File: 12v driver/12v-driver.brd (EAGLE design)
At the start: 60.9 x 77.1 mm, 36 parts, among them IC1 74AC14N, IC2 74AC14N, Q1 2N3906, Q2 2N3906, Q3 IRFPC40, Q4 IRFPC40, T1 2N3904, T2 2N3904, T3 2N3904, T4 2N3904

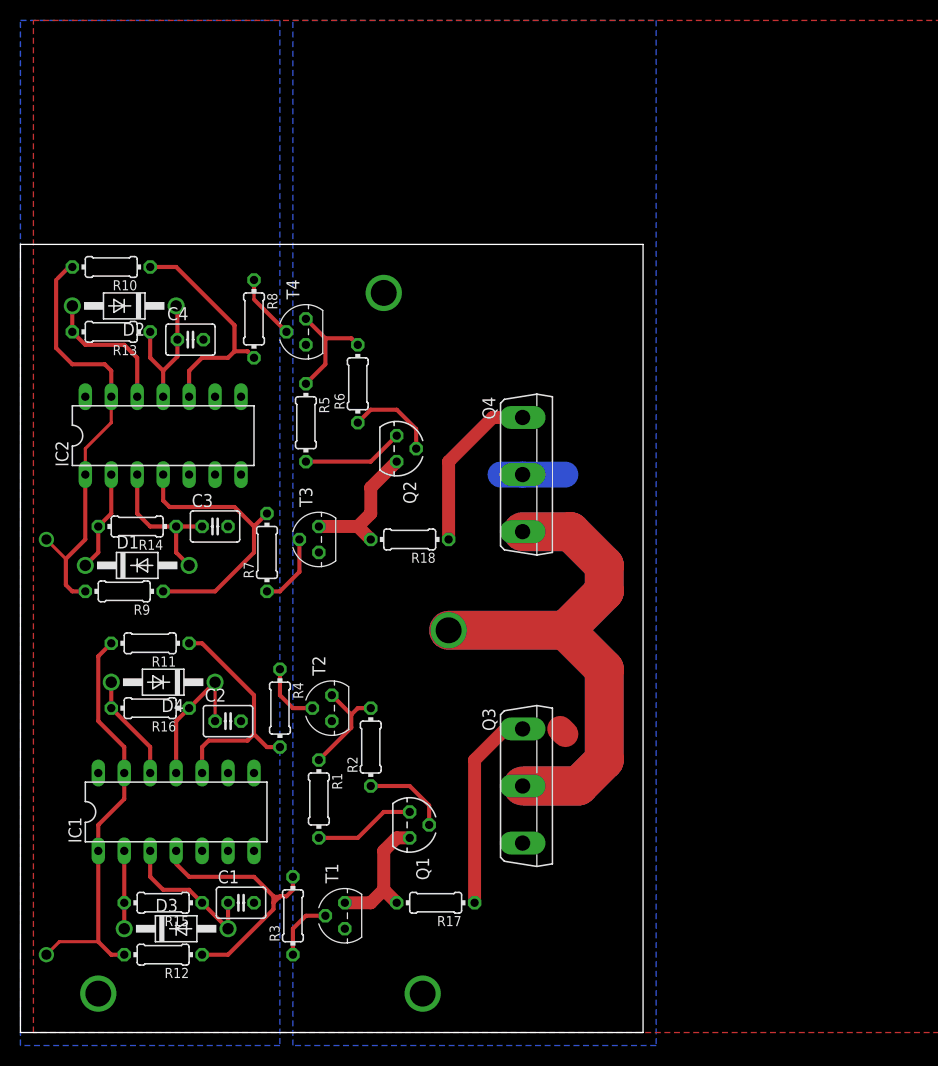
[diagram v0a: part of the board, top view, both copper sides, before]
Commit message: 12driver fix inversion and SMD
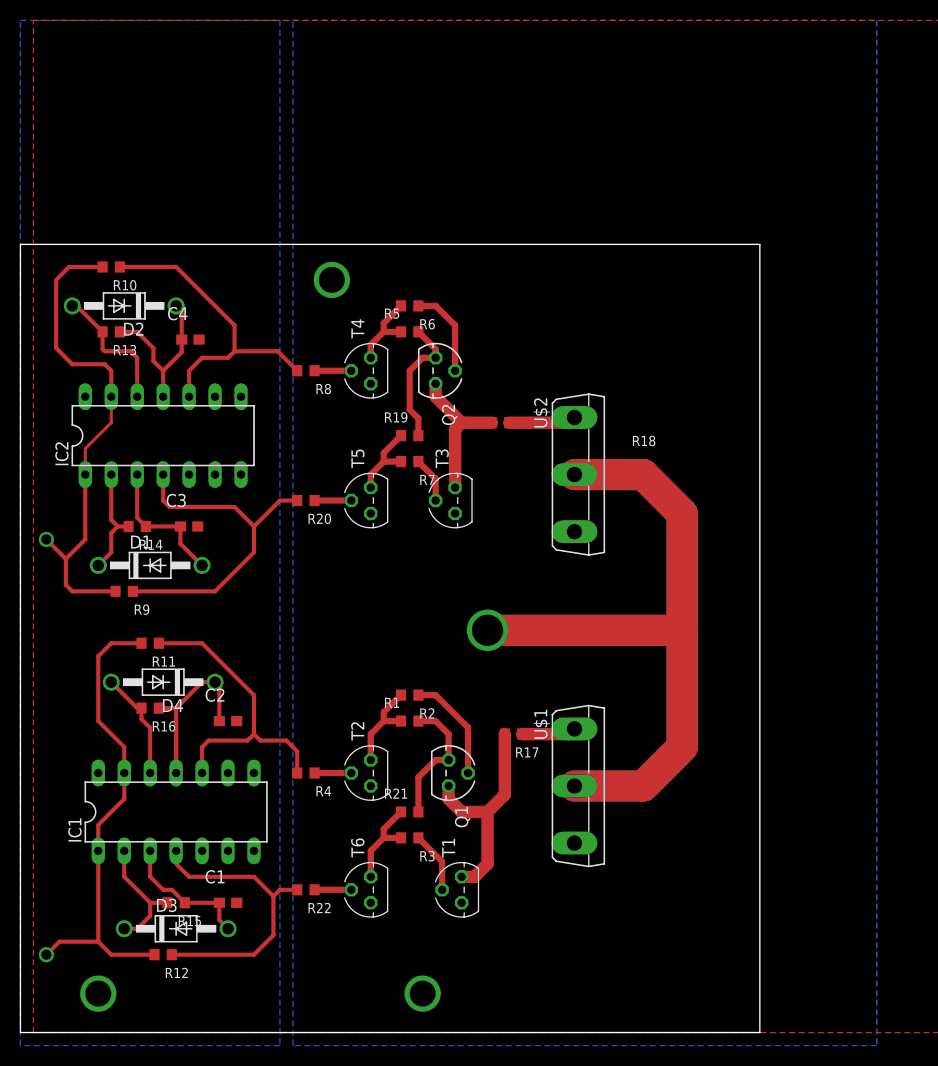
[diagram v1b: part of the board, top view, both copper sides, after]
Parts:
- removed Q3, Q4: IRFPC40, transistor-power:TO247BV
- added R19, R20, R21, R22: 1k, rcl:R0603
- added T5, T6: 2N3904, transistor:TO92
- added U$1: N-CHANNEL, transistors:TO247BV
- added U$2: P-CHANNEL, transistors:TO247BV
- C1, C2, C3, C4: device rcl:C025-030X050 -> rcl:C0603
- R1, R10, R11, R12, R13, R14, R15, R16, R17, R18, R2, R3, R4, R5, R6, R7, R8, R9: device rcl:0204/7 -> rcl:R0603
- moved R17 18.2 mm to (39.4, 29.2)
- moved R7 16.6 mm to (29.2, 55.9), turned to 180 degrees
- moved R18 14.5 mm to (38.1, 59.7)
- moved T3 13.9 mm to (33.7, 52.1)
- moved R3 13.7 mm to (29.2, 19.1), turned to 180 degrees
- moved R5 13.5 mm to (29.2, 68.6), turned to 0 degrees
- moved R1 11.7 mm to (29.2, 30.5), turned to 0 degrees
- moved T1 11.7 mm to (34.3, 14.0)
- moved R6 9.16 mm to (29.2, 71.1), turned to 180 degrees
- moved Q2 8.52 mm to (31.8, 64.8)
- moved T2 7.41 mm to (25.4, 25.4)
- moved T4 7.41 mm to (25.4, 64.8)
- moved R8 7.18 mm to (19.1, 64.8), turned to 180 degrees
- moved R4 6.84 mm to (19.1, 25.4), turned to 180 degrees
- moved R2 6.35 mm to (29.2, 33.0), turned to 180 degrees
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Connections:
- new net N$15: R20.1, T5.2
- new net N$24: R22.1, T6.2
- new net N$27: R19.1, R7.2, T5.1
- new net N$28: R21.1, R3.2, T6.1
- net GND: now also T5.3, T6.3, U$1.S; no longer Q3.S
- net N$14: now also R22.2; no longer R3.2
- net N$19: now also R20.2; no longer R7.2
- net N$2: now also U$1.G; no longer Q3.G
- net N$8: now also U$2.G; no longer Q4.G
- net OUTPUT: now also U$1.D, U$2.D; no longer Q3.D, Q4.S
- net V+: now also R19.2, R21.2, U$2.S; no longer Q4.D
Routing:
- net OUTPUT: track 104.1 -> 132.3 mm
- net N$2: track 19.9 -> 5.33 mm
- net N$8: track 16.6 -> 6.60 mm
- net N$28: track 0.00 -> 9.27 mm
- net N$1: track 13.0 -> 22.1 mm
- net N$27: track 0.00 -> 8.00 mm
- net N$21: track 23.1 -> 30.8 mm
- net N$16: track 14.3 -> 22.0 mm
- net N$17: track 23.5 -> 30.4 mm
- net N$19: track 27.3 -> 33.7 mm
- net IN2: track 42.8 -> 48.7 mm
- net IN1: track 40.5 -> 46.4 mm
- net N$25: track 7.62 -> 12.2 mm
- net N$24: track 0.00 -> 3.60 mm
- net N$15: track 0.00 -> 3.60 mm
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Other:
- board size 60.9 x 77.1 mm -> 72.4 x 77.1 mm

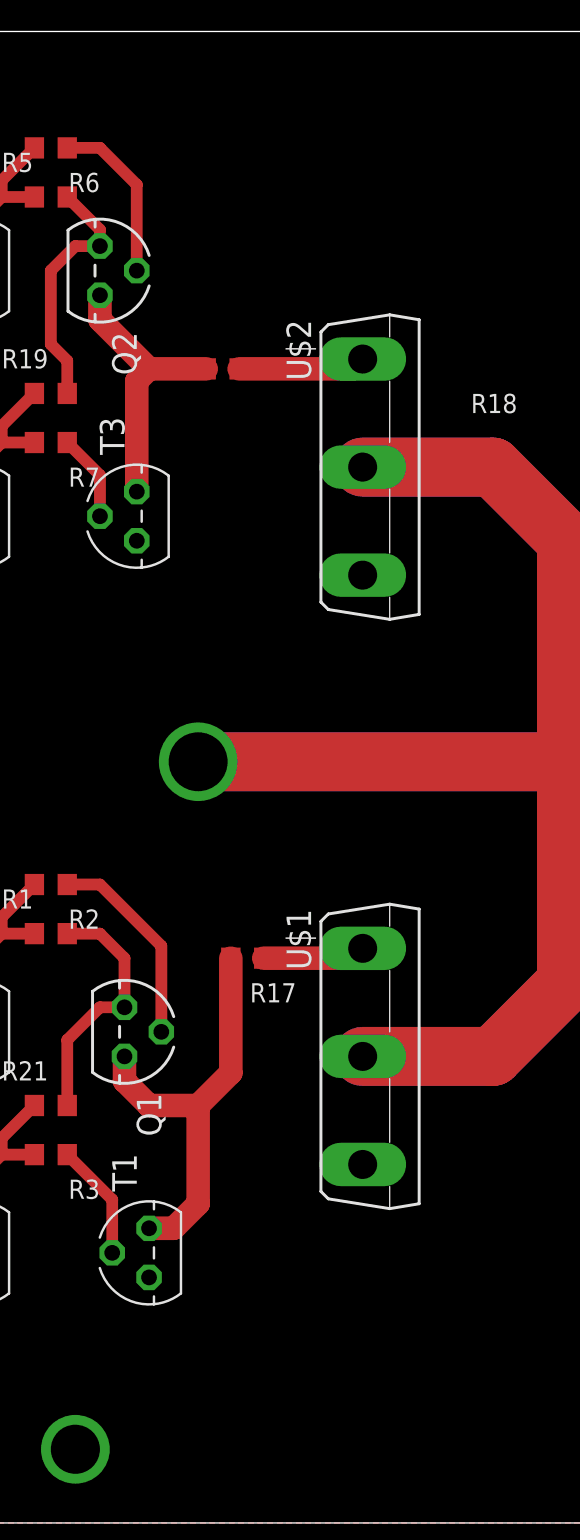
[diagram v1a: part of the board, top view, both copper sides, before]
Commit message: added inverter to driver NPNs
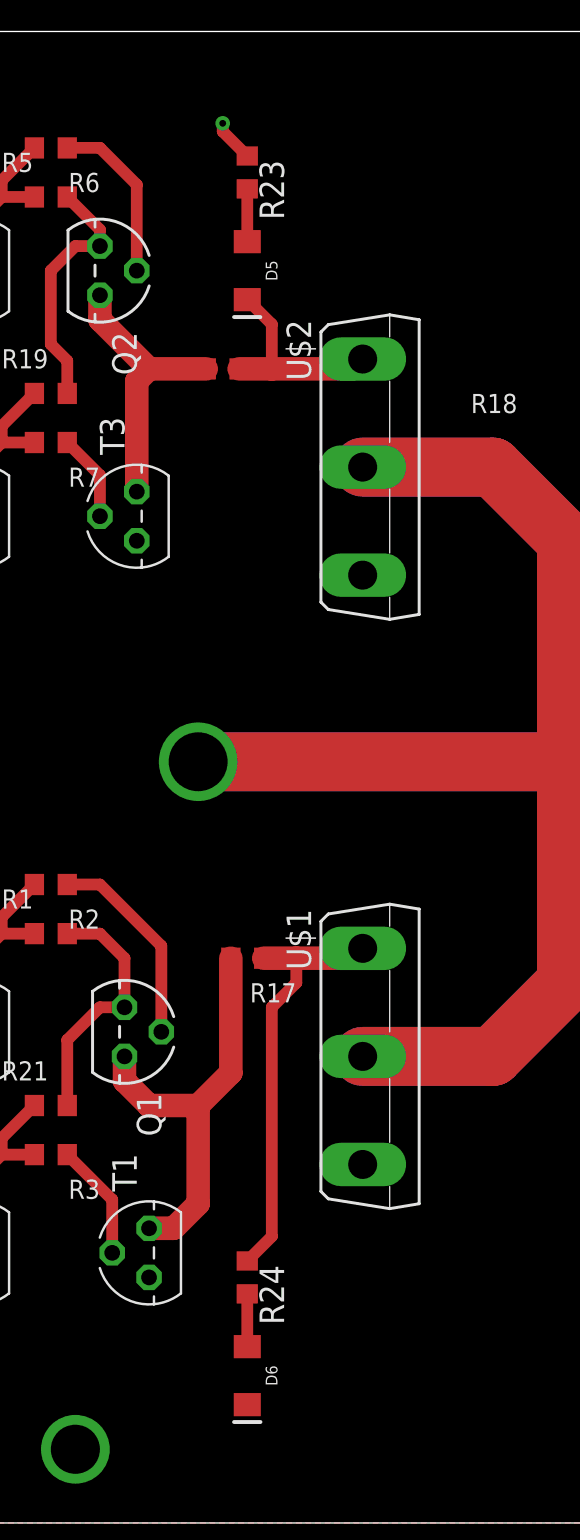
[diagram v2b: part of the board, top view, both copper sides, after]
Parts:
- added D5, D6: WHITE, SparkFun-LED:LED-1206
- added R23, R24: 5k, rcl:R0603
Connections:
- new net N$29: D5.A, R23.2
- new net N$30: D6.A, R24.2
- net GND: now also D6.C
- net N$2: now also R24.1
- net N$8: now also D5.C
- net V+: now also R23.1
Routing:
- net N$2: track 5.33 -> 22.0 mm
- net N$8: track 6.60 -> 10.7 mm
- net N$29: track 0.00 -> 2.73 mm
- net N$30: track 0.00 -> 2.73 mm
- net V+: track 26.1 -> 28.3 mm, vias 1 -> 2

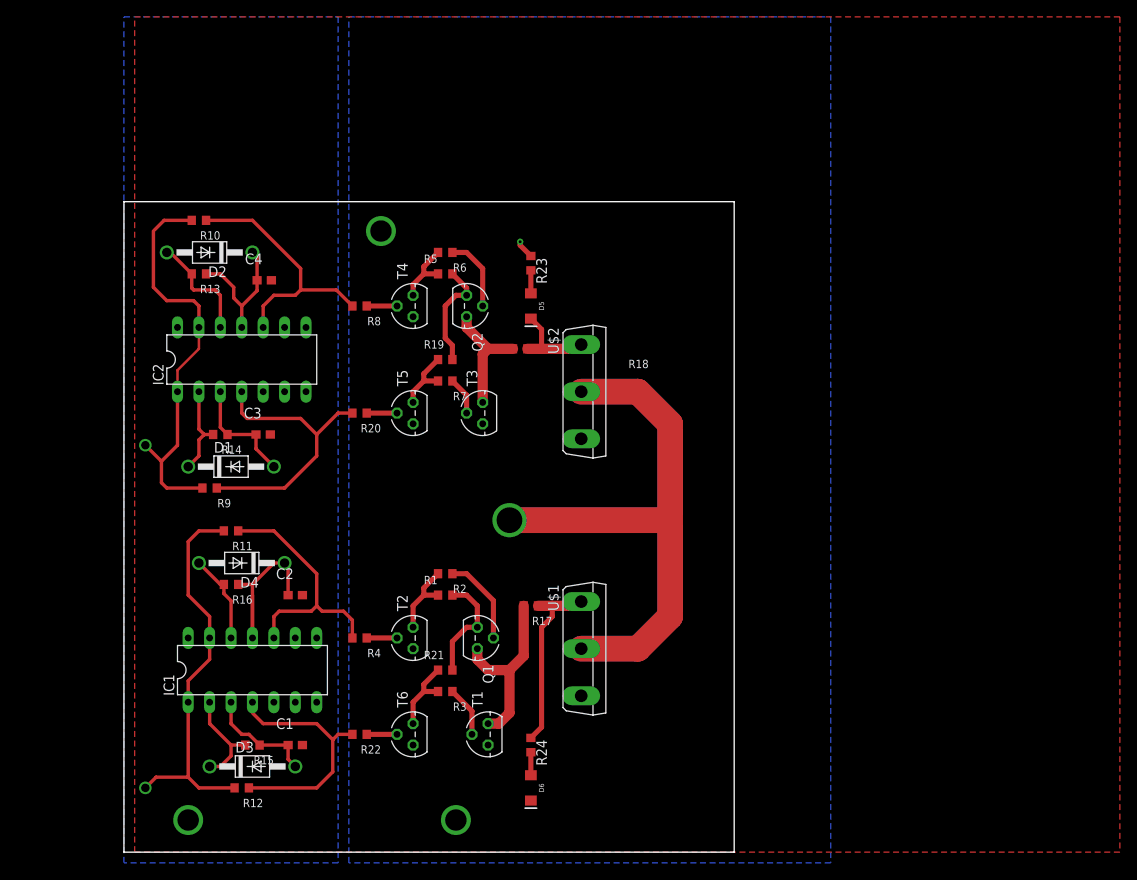
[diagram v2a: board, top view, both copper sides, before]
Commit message: fixed production problems
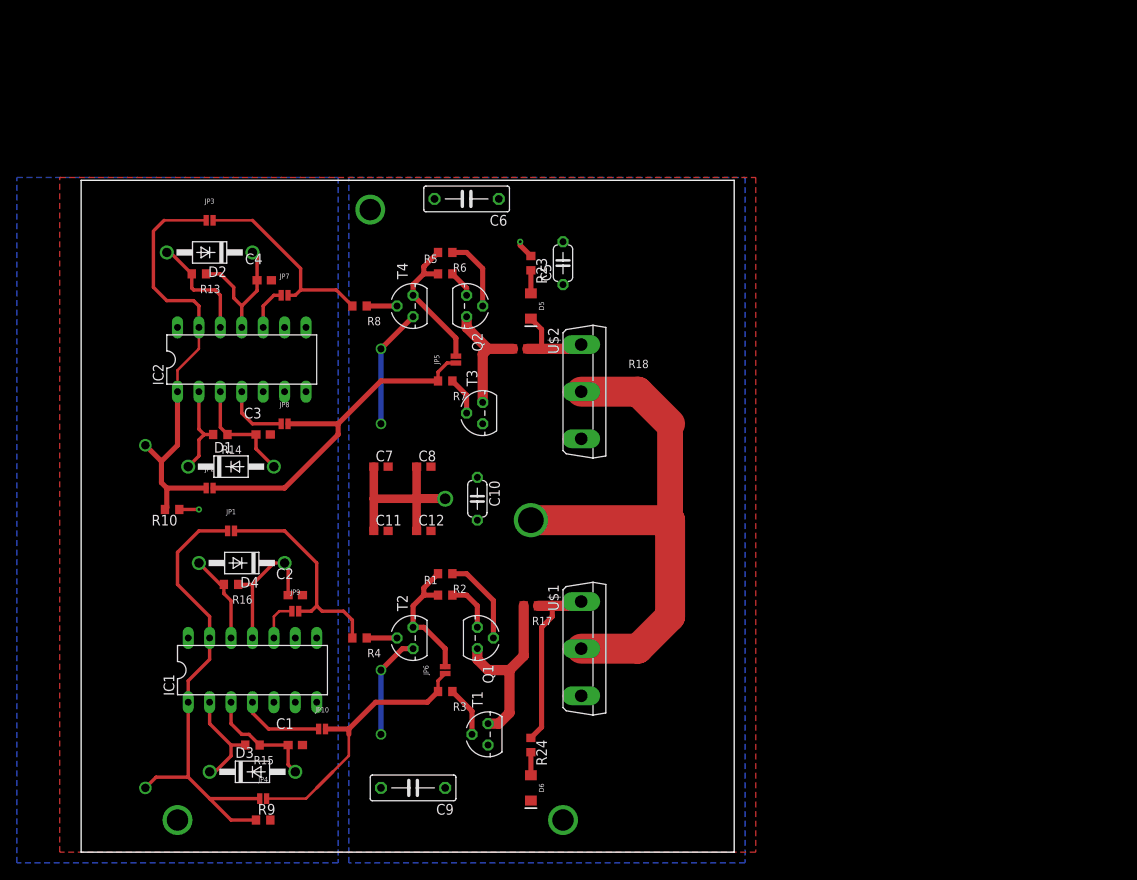
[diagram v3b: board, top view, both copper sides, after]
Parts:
- removed R11, R12: 0r, rcl:R0603
- removed R19, R20, R21, R22: 1k, rcl:R0603
- removed T5, T6: 2N3904, transistor:TO92
- added C10, C5: (no value), rcl:C050-024X044
- added C11, C12, C7, C8: (no value), rcl:C0603
- added C6, C9: (no value), rcl:C075-032X103
- added JP1, JP10, JP2, JP3, JP4, JP5, JP6, JP7, JP8, JP9: JUMPER-SMT_2_NO_NO-SILK, SparkFun-Jumpers:SMT-JUMPER_2_NO_NO-SILK
- R10: value 0r -> 2k
- R9: value 0r -> 1k
- moved R9 39.9 mm to (7.62, 3.81), turned to 0 degrees
- moved R10 34.4 mm to (-3.17, 40.6)
- moved D3 0.63 mm to (6.35, 9.53)
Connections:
- net +5V: now also R10.1
- net GND: now also C10.2, C11.2, C12.2, C5.2, C6.2, C7.2, C8.2, C9.2, R9.2; no longer T5.3, T6.3
- net IN1: now also JP1.1, JP4.1, R9.1; no longer R11.2, R12.2
- net IN2: now also JP2.1, JP3.1; no longer R9.2
- net N$14: now also IC2.10, JP7.1; no longer IC1.4, R12.1, R22.2
- net N$15: now also JP2.2, JP5.1, JP8.2, R7.2; no longer R20.1, T5.2
- net N$17: now also JP1.2, JP9.2; no longer IC1.10, R11.1
- net N$19: now also JP8.1; no longer R20.2, R9.1
- net N$21: now also JP3.2, JP7.2; no longer IC2.10, R10.1
- net N$24: now also IC1.10, JP9.1; no longer R22.1, T6.2
- net N$27: now also IC1.4, JP10.1; no longer R19.1, R7.2, T5.1
- net N$28: now also JP10.2, JP4.2, JP6.1; no longer R21.1, T6.1
- net N$3: now also JP6.2
- net N$9: now also JP5.2
- net V+: now also C10.1, C11.1, C12.1, C5.1, C6.1, C7.1, C8.1, C9.1; no longer R19.2, R21.2
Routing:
- net N$15: track 3.60 -> 42.3 mm
- net GND: track 0.00 -> 26.8 mm, vias 1 -> 5
- net N$19: track 33.7 -> 7.74 mm
- net N$14: track 29.2 -> 5.20 mm
- net N$28: track 9.27 -> 32.7 mm
- net IN1: track 46.4 -> 58.0 mm
- net V+: track 28.3 -> 38.6 mm, vias 2 -> 3
- net N$9: track 8.00 -> 17.3 mm
- net N$3: track 9.27 -> 16.3 mm
- net N$21: track 30.8 -> 24.0 mm
- net OUTPUT: track 132.3 -> 127.2 mm
- net N$16: track 22.0 -> 16.9 mm
- net IN2: track 48.7 -> 53.5 mm
- net N$17: track 30.4 -> 25.9 mm
- net +5V: track 0.00 -> 2.33 mm, vias 1 -> 2
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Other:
- board size 72.4 x 77.1 mm -> 77.5 x 79.7 mm

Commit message: started rework of new schematic
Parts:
- removed IC2: 74AC14N, 74xx-eu:DIL14
- removed JP5, JP6: JUMPER-SMT_2_NO_NO-SILK, SparkFun-Jumpers:SMT-JUMPER_2_NO_NO-SILK
- removed T2, T3, T4: 2N3904, transistor:TO92
- added C13, C14, C15, C16: (no value), rcl:C0603
- added D10, D11, D12, D7, D8, D9: (no value), diode:DO-214AC
- added IC3: 4081N, 40xx:DIL14
- added IC4: 74AC14D, 74xx-eu:SO14
- added Q10, Q9: (no value), adafruit:SOT23
- added Q11, Q12: BSS84, Transistor:SOT23
- added Q13: 2N2907, adafruit:TO92-EBC-OVAL
- added Q3, Q4, Q5, Q6, Q7, Q8: BC618, transistor-npn:TO92-EBC
- added R11, R12, R19, R20: 1k, rcl:R0603
- added R21, R22, R25: 30r, rcl:R0603
- added U$3: STM32F070F6P6TR, Capstone:TSSOP20
- D1, D2, D3, D4: value 1N4004 -> (none); device diode:DO41-10 -> diode:DO-214AC
- IC1: value 74AC14N -> 74AC14D; device 74xx-eu:DIL14 -> 74xx-eu:SO14
- Q1, Q2: value 2N3906 -> BC618; device transistor-pnp:TO92 -> transistor-npn:TO92-EBC
- R17: value 30r -> 2k
- R2, R3: value 500r -> 300r
- R23, R24: value 5k -> 10k
- T1: value 2N3904 -> 2N2222; device transistor:TO92 -> adafruit:TO92-EBC-OVAL
- moved T1 339.7 mm to (-196.8, -234.9), turned to 0 degrees
- moved Q2 314.7 mm to (-110.5, -215.9), turned to 0 degrees
- moved Q1 276.3 mm to (-101.6, -215.9), turned to 0 degrees
- moved IC1 243.5 mm to (-90.2, -201.9)
- moved D2 192.7 mm to (-17.8, -120.7), turned to 0 degrees
- moved D1 174.1 mm to (-17.8, -127.0)
- moved D4 169.2 mm to (-17.8, -133.3), turned to 0 degrees
- moved R18 154.5 mm to (-19.1, -83.8), turned to 0 degrees
- moved D3 151.2 mm to (-17.8, -139.7)
- moved R17 143.3 mm to (-19.1, -101.6), turned to 0 degrees
- moved C3 50.8 mm to (58.4, 49.5)
- moved C5 50.8 mm to (94.0, 69.8)
- moved C9 50.8 mm to (76.2, 7.62)
- moved D5 50.8 mm to (90.2, 64.8)
- moved D6 50.8 mm to (90.2, 7.62)
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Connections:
- removed net +5V: IC1.14, IC2.14, R10.1
- new net +3V3: IC1.14, IC4.14, R10.1, U$3.16, U$3.5
- new net ADC1: U$3.6
- new net ADC2: U$3.7
- new net ADC3: U$3.8
- new net ENABLE1: U$3.18
- new net ENABLE2: U$3.17
- new net ENABLE3: U$3.11
- new net HALF_VCC: U$3.9
- new net IN: Q13.B, T1.B
- new net N$31: C16.2, Q8.B, R12.1
- new net N$32: D12.C, Q7.B, Q8.C, R11.1
- new net N$33: C14.2, Q4.B, R20.1
- new net N$34: C14.1, JP2.2, JP8.2, R20.2
- new net N$35: D10.C, Q3.B, Q4.C, R19.1
- new net N$36: IC1.13, IC3.2
- new net N$37: IC3.1, IC3.6
- new net N$38: IC3.3, IC4.13
- new net N$39: U$3.4
- new net N$40: Q12.3, R21.1
- new net N$41: D5.C, Q10.3, R22.2
- new net N$42: Q9.3, R25.2
- new net N$43: D9.A, Q1.E, R6.2
- new net N$44: D10.A, Q3.E, R7.2
- new net N$47: D11.A, Q5.E, R2.2
- new net N$48: D12.A, Q7.E, R3.2
- new net OUT: Q13.E, T1.E
- new net PWM1: U$3.14
- new net PWM2: U$3.13
- new net PWM3: U$3.12
- new net SWCLK: U$3.20
- new net SWDIO: U$3.19
- new net VDD: IC3.14
- new net VSS: IC3.7
- net GND: now also D8.A, IC4.7, Q10.2, Q13.C, Q2.E, Q4.E, Q6.E, Q8.E, Q9.2, R17.1, U$3.15; no longer IC2.7, T1.3, T2.3, T3.3, T4.3
- net IN1: now also IC1.11, IC1.3, IC3.4; no longer IC1.1, IC1.13
- net IN2: now also IC4.11, IC4.12, IC4.3; no longer IC2.1, IC2.13
- net N$1: now also R18.2, R25.1, U$1.G; no longer Q1.1, R17.2, T1.1
- net N$10: now also Q12.1; no longer Q2.2
- net N$11: now also Q10.1; no longer T3.2
- net N$12: now also C13.2, Q2.B; no longer T4.2
- net N$13: now also IC1.10; no longer IC1.12
- net N$14: now also IC4.8; no longer IC2.10
- net N$15: now also IC1.12, IC3.5; no longer JP2.2, JP5.1, JP8.2, R7.2
- net N$16: now also IC1.9; no longer IC1.11
- net N$17: now also C15.1
- net N$18: now also IC4.5; no longer IC2.3
- net N$19: now also IC4.6; no longer IC2.4
- net N$2: now also R17.2, U$3.1; no longer R17.1, R24.1, U$1.G
- net N$20: now also IC4.9; no longer IC2.11
- net N$21: now also C13.1
- net N$22: now also IC4.10; no longer IC2.12
- net N$23: now also IC4.4; no longer IC2.2
- net N$24: now also IC1.8; no longer IC1.10
- net N$25: now also IC1.4; no longer IC1.2
- net N$26: now also IC1.5; no longer IC1.3
- net N$27: now also IC1.6; no longer IC1.4
- net N$28: now also C16.1, R12.2; no longer JP6.1, R3.2
- net N$3: now also D11.C, Q5.B, Q6.C; no longer JP6.2, R2.2, T2.1
- net N$4: now also Q11.1; no longer Q1.2
- net N$5: no longer T1.2
- net N$6: now also C15.2, Q6.B; no longer T2.2
- net N$7: now also R21.2, R22.1, U$2.G; no longer Q2.1, R18.2, T3.1
- net N$8: now also Q11.3, R24.1; no longer D5.C, U$2.G
- net N$9: now also D9.C, Q1.B, Q2.C; no longer JP5.2, R6.2, T4.1
- net OUTPUT: now also D7.A, D8.C
- net V+: now also D7.C, Q1.C, Q11.2, Q12.2, Q3.C, Q5.C, Q7.C, R11.2, R19.2, T1.C; no longer Q1.3, Q2.3
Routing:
- net OUTPUT: track 127.2 -> 0.00 mm
- net N$15: track 42.3 -> 0.00 mm
- net N$34: track 0.00 -> 31.9 mm
- net GND: track 26.8 -> 0.00 mm, vias 5 -> 1
- net N$2: track 22.0 -> 0.00 mm
- net IN1: track 58.0 -> 37.9 mm
- net IN2: track 53.5 -> 35.9 mm
- net N$9: track 17.3 -> 4.34 mm
- net N$3: track 16.3 -> 4.34 mm
- net N$8: track 10.7 -> 0.00 mm
- net N$16: track 16.9 -> 8.67 mm
- net N$13: track 10.7 -> 2.70 mm
- net N$18: track 13.5 -> 6.27 mm
- net N$7: track 14.4 -> 7.22 mm
- net N$23: track 11.0 -> 4.76 mm
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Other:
- board size 77.5 x 79.7 mm -> 100 x 100 mm
